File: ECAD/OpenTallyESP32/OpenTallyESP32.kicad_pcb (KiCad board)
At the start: 2 copper layers, 42 x 29 mm, 11 parts, among them J1 Conn_01x02, Q1 AO3400A, SW1 SW_Push, U1 XIAO ESP32C3

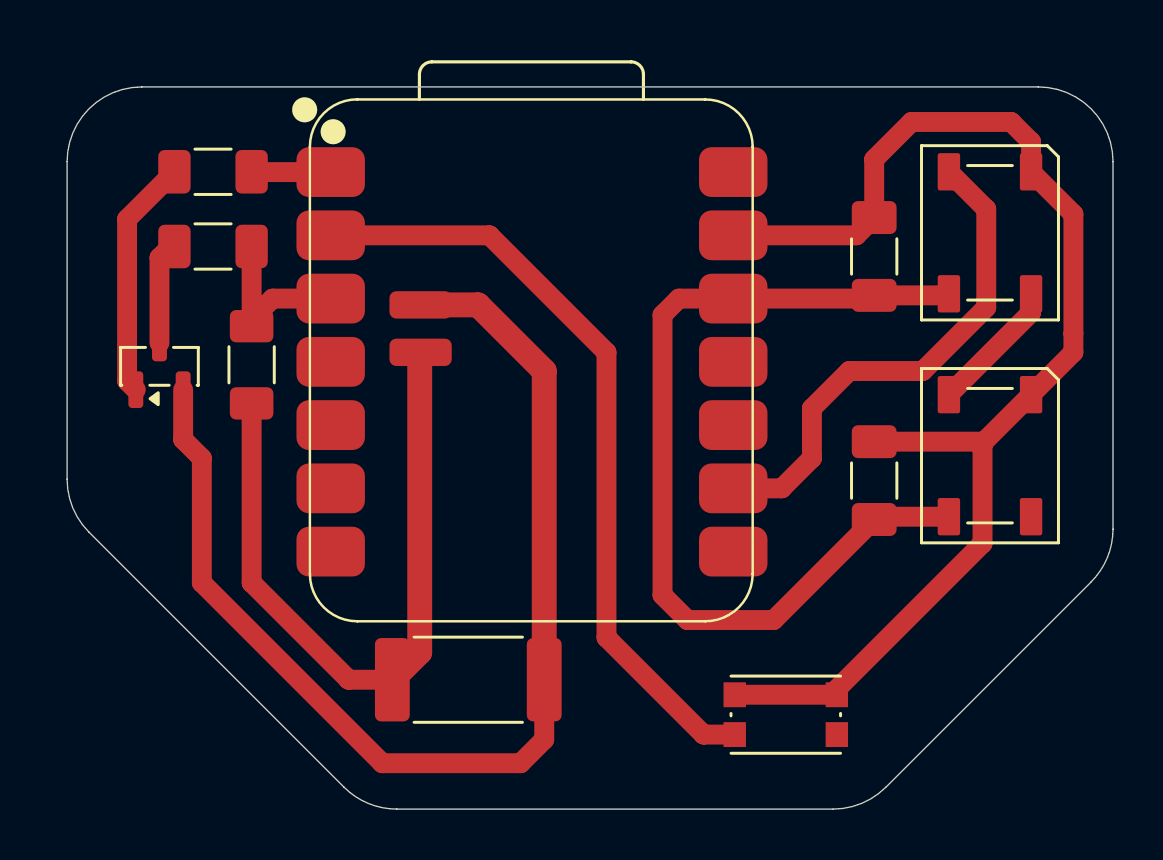
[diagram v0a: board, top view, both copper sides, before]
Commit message: Moved battery solder pads and minor tweaks to routing
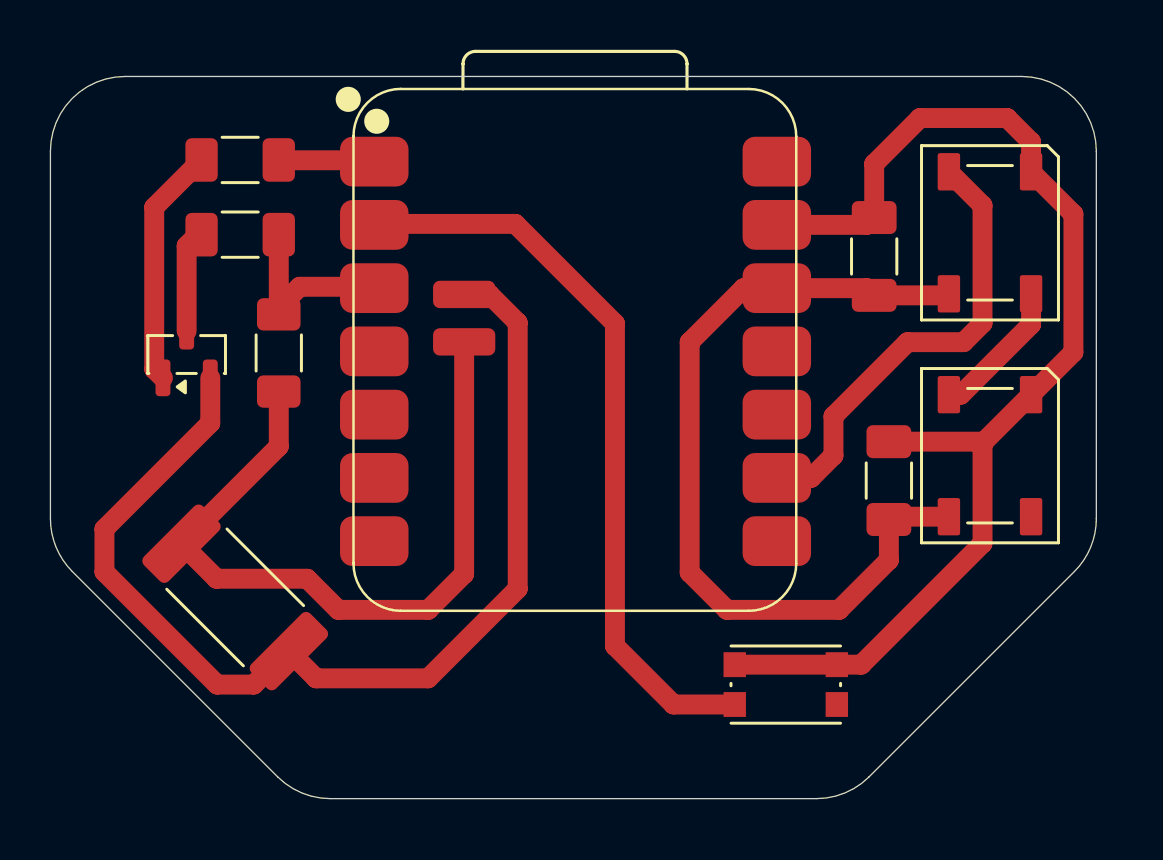
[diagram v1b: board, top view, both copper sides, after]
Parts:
- moved J1 9.93 mm to (56.8, 66.5), turned to 135 degrees
- moved U1 1.80 mm to (61.5, 67.1)
- moved SW1 1.21 mm to (78.9, 70.0)
- moved R1 1.19 mm to (58.5, 56.7)
- moved R2 1.19 mm to (57.0, 51.9)
- moved R3 1.19 mm to (57.0, 48.9)
- moved Q1 1.19 mm to (54.8, 56.7)
- moved C2 0.59 mm to (83.0, 61.8)
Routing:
- net GND: track 50.8 -> 47.8 mm
- net +3.3V: track 36.7 -> 34.4 mm
- net -BATT: track 46.1 -> 43.8 mm
- net NEOPIXEL: track 20.4 -> 18.4 mm
- net +BATT: track 28.1 -> 30.1 mm
- net SW: track 31.5 -> 30.1 mm
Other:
- outline, holes or cut-outs redrawn
